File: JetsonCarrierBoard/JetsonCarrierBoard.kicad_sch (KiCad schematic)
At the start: 0 parts

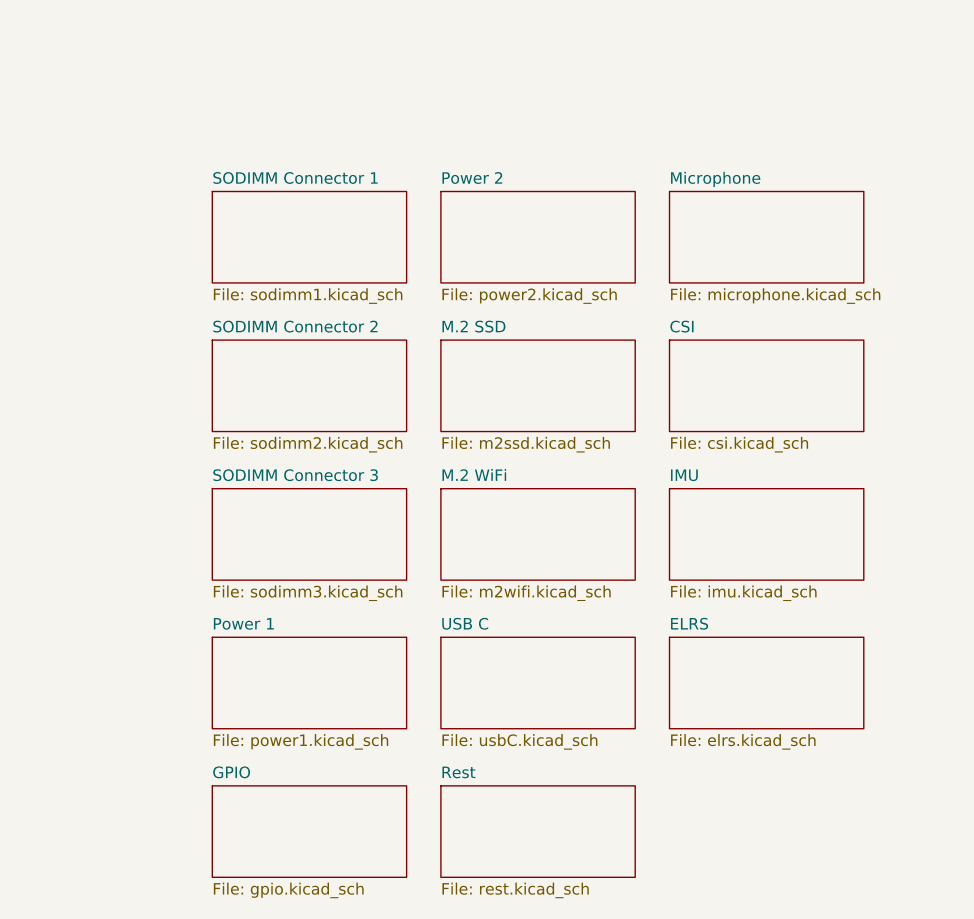
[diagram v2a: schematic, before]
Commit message: Part 2 of USB C wiring, renaming schematics
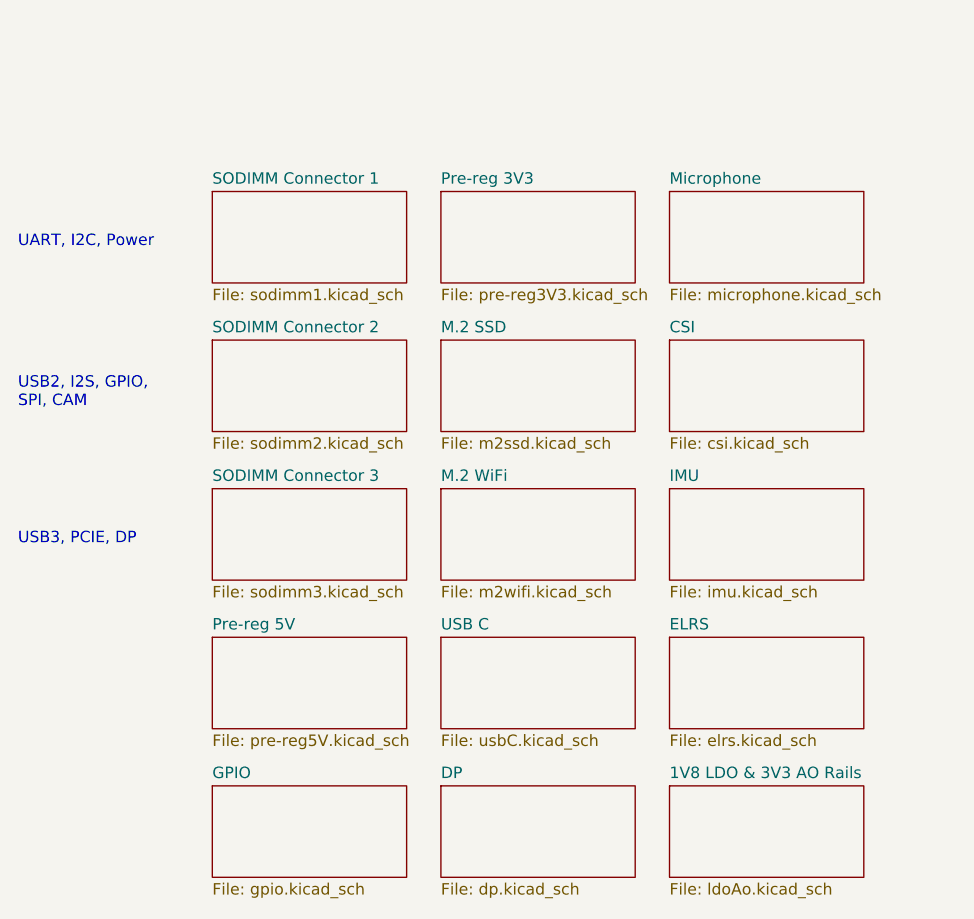
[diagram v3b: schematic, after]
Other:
- sheet Power 1 renamed Pre-reg 5V
- sheet Power 2 renamed Pre-reg 3V3
- sheet Rest renamed DP
- added sheet 1V8 LDO & 3V3 AO Rails (ldoAo.kicad_sch)
- sheet DP: file rest.kicad_sch -> dp.kicad_sch
- sheet Pre-reg 3V3: file power2.kicad_sch -> pre-reg3V3.kicad_sch
- sheet Pre-reg 5V: file power1.kicad_sch -> pre-reg5V.kicad_sch
- note added: "UART, I2C, Power"
- note added: "USB2, I2S, GPIO, SPI, CAM"
- note added: "USB3, PCIE, DP"
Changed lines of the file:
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@@
 (kicad_sch (version 20211123) (generator eeschema)
   (paper "A4")
+  (text "USB2, I2S, GPIO,\nSPI, CAM" (at 95.25 85.09 0)
+    (effects (font (size 1.27 1.27)) (justify left bottom))
+  )
+  (text "USB3, PCIE, DP" (at 95.25 100.33 0)
+    (effects (font (size 1.27 1.27)) (justify left bottom))
+  )
+  (text "UART, I2C, Power" (at 95.25 67.31 0)
+    (effects (font (size 1.27 1.27)) (justify left bottom))
+  )
   (sheet (at 142.24 110.49) (size 21.59 10.16) (fields_autoplaced)
     (stroke (width 0.1524) (type solid) (color 0 0 0 0))
@@
     (stroke (width 0.1524) (type solid) (color 0 0 0 0))
     (fill (color 0 0 0 0.0000))
-    (property "Sheet name" "Rest" (id 0) (at 142.24 126.2884 0)
-      (effects (font (size 1.27 1.27)) (justify left bottom))
-    )
-    (property "Sheet file" "rest.kicad_sch" (id 1) (at 142.24 137.7446 0)
+    (property "Sheet name" "DP" (id 0) (at 142.24 126.2884 0)
+      (effects (font (size 1.27 1.27)) (justify left bottom))
+    )
+    (property "Sheet file" "dp.kicad_sch" (id 1) (at 142.24 137.7446 0)
       (effects (font (size 1.27 1.27)) (justify left top))
     )
@@
     (stroke (width 0.1524) (type solid) (color 0 0 0 0))
     (fill (color 0 0 0 0.0000))
-    (property "Sheet name" "Power 2" (id 0) (at 142.24 60.2484 0)
-      (effects (font (size 1.27 1.27)) (justify left bottom))
-    )
-    (property "Sheet file" "power2.kicad_sch" (id 1) (at 142.24 71.7046 0)
+    (property "Sheet name" "Pre-reg 3V3" (id 0) (at 142.24 60.2484 0)
+      (effects (font (size 1.27 1.27)) (justify left bottom))
+    )
+    (property "Sheet file" "pre-reg3V3.kicad_sch" (id 1) (at 142.24 71.7046 0)
       (effects (font (size 1.27 1.27)) (justify left top))
     )
@@
     (stroke (width 0.1524) (type solid) (color 0 0 0 0))
     (fill (color 0 0 0 0.0000))
-    (property "Sheet name" "Power 1" (id 0) (at 116.84 109.7784 0)
-      (effects (font (size 1.27 1.27)) (justify left bottom))
-    )
-    (property "Sheet file" "power1.kicad_sch" (id 1) (at 116.84 121.2346 0)
+    (property "Sheet name" "Pre-reg 5V" (id 0) (at 116.84 109.7784 0)
+      (effects (font (size 1.27 1.27)) (justify left bottom))
+    )
+    (property "Sheet file" "pre-reg5V.kicad_sch" (id 1) (at 116.84 121.2346 0)
       (effects (font (size 1.27 1.27)) (justify left top))
     )
@@
     )
     (property "Sheet file" "csi.kicad_sch" (id 1) (at 167.64 88.2146 0)
+      (effects (font (size 1.27 1.27)) (justify left top))
+    )
+  )
+  (sheet (at 167.64 127) (size 21.59 10.16) (fields_autoplaced)
+    (stroke (width 0.1524) (type solid) (color 0 0 0 0))
+    (fill (color 0 0 0 0.0000))
+    (property "Sheet name" "1V8 LDO & 3V3 AO Rails" (id 0) (at 167.64 126.2884 0)
+      (effects (font (size 1.27 1.27)) (justify left bottom))
+    )
+    (property "Sheet file" "ldoAo.kicad_sch" (id 1) (at 167.64 137.7446 0)
       (effects (font (size 1.27 1.27)) (justify left top))
     )
@@
     (path "/6dd6e531-721a-4414-9cf5-a3390f309250" (page "14"))
     (path "/35a02f26-4e5e-4a54-87ef-75964a5a411a" (page "15"))
+    (path "/c4aedfda-3c53-45a7-9372-54b9a8f840ba" (page "16"))
   )
   (symbol_instances
-    (path "/7661caa5-a831-4a38-b30b-4546d9bcecdf/0697383b-caf2-42af-bc6d-3eec7a8e6e3d"
-      (reference "#PWR?") (unit 1) (value "+1V8") (footprint "")
-    )
     (path "/c4d380ca-b1d9-4a41-86cf-2b0a86998e0d/09e60d52-849d-4e9f-ae3f-e84e48e8dc21"
       (reference "#PWR?") (unit 1) (value "GND") (footprint "")
@@
     (path "/963f32ba-ec92-4ff1-85dd-63f258059e2d/1386d9a4-71f7-41cd-a560-524abed48850"
       (reference "#PWR?") (unit 1) (value "GND") (footprint "")
+    )
+    (path "/05070324-6f97-4cc0-bdcf-f69bfad6a219/15a6b218-6239-4a6b-9613-e6139914a5c6"
+      (reference "#PWR?") (unit 1) (value "+3.3V") (footprint "")
     )
     (path "/7661caa5-a831-4a38-b30b-4546d9bcecdf/1fae16da-9009-4d63-a296-eaa85652b15b"
@@
       (reference "#PWR?") (unit 1) (value "+3.3V") (footprint "")
     )
-    (path "/7661caa5-a831-4a38-b30b-4546d9bcecdf/5a60a596-f969-4048-b9f0-6c28b54abd9a"
-      (reference "#PWR?") (unit 1) (value "+3.3V") (footprint "")
+    (path "/c4aedfda-3c53-45a7-9372-54b9a8f840ba/5a2d866f-dcb6-43a7-97d0-a02698ce52e6"
+      (reference "#PWR?") (unit 1) (value "+1V8") (footprint "")
+    )
+    (path "/05070324-6f97-4cc0-bdcf-f69bfad6a219/6bda150f-3a32-40ae-a0f8-d9012a1832bc"
+      (reference "#PWR?") (unit 1) (value "GND") (footprint "")
     )
     (path "/7661caa5-a831-4a38-b30b-4546d9bcecdf/75b2df67-f1c8-4922-a8d4-5d0eb1b6eea4"
@@
       (reference "#PWR?") (unit 1) (value "GND") (footprint "")
     )
+    (path "/c4aedfda-3c53-45a7-9372-54b9a8f840ba/bb59e28f-2c75-4121-9867-d2dc70664f7f"
+      (reference "#PWR?") (unit 1) (value "+3.3V") (footprint "")
+    )
+    (path "/c4aedfda-3c53-45a7-9372-54b9a8f840ba/bc7ccac9-6e56-4a2c-bf25-4c95c1121299"
+      (reference "#PWR?") (unit 1) (value "GND") (footprint "")
+    )
     (path "/a2d05d86-0e9b-47b0-b97a-14889aed3931/cf739241-7f9e-4bd9-84c7-298a551b760f"
       (reference "#PWR?") (unit 1) (value "GND") (footprint "")
     )
-    (path "/7661caa5-a831-4a38-b30b-4546d9bcecdf/d0f9fc88-e77e-4f80-bfd3-6861f27fa879"
-      (reference "#PWR?") (unit 1) (value "GND") (footprint "")
-    )
     (path "/fd522664-18f7-41a9-83db-3444870594c0/d424cdad-6034-4fd4-a3b2-c8c7189615cb"
       (reference "#PWR?") (unit 1) (value "GND") (footprint "")
@@
     )
     (path "/05070324-6f97-4cc0-bdcf-f69bfad6a219/e0363390-9312-4b3d-9173-324d0cb811d4"
+      (reference "#PWR?") (unit 1) (value "GND") (footprint "")
+    )
+    (path "/05070324-6f97-4cc0-bdcf-f69bfad6a219/e41ed448-34b7-423b-b572-8fa8b01887a9"
       (reference "#PWR?") (unit 1) (value "GND") (footprint "")
     )
@@
       (reference "C?") (unit 1) (value "0.1u") (footprint "")
     )
+    (path "/05070324-6f97-4cc0-bdcf-f69bfad6a219/4e2886bd-49ab-4698-a872-da0d7e10c965"
+      (reference "C?") (unit 1) (value "C") (footprint "")
+    )
     (path "/c4d380ca-b1d9-4a41-86cf-2b0a86998e0d/616c44f2-bc9f-4390-a1e7-a0df954ba2ec"
       (reference "C?") (unit 1) (value "0.22u") (footprint "")
@@
       (reference "C?") (unit 1) (value "22u") (footprint "")
     )
+    (path "/05070324-6f97-4cc0-bdcf-f69bfad6a219/cae4f632-e432-407a-8bf7-a0a99da561ba"
+      (reference "C?") (unit 1) (value "C") (footprint "")
+    )
     (path "/a2d05d86-0e9b-47b0-b97a-14889aed3931/cca040ec-e059-44dd-956f-79e8ab13c13d"
       (reference "C?") (unit 1) (value "22u") (footprint "")
@@
       (reference "C?") (unit 1) (value "4.7u") (footprint "")
     )
+    (path "/05070324-6f97-4cc0-bdcf-f69bfad6a219/ff8b12bf-4a69-4259-b1f0-038968ec0374"
+      (reference "C?") (unit 1) (value "C") (footprint "")
+    )
+    (path "/05070324-6f97-4cc0-bdcf-f69bfad6a219/ffd2a1ff-3a78-4139-a444-76d5257a8546"
+      (reference "C?") (unit 1) (value "C") (footprint "")
+    )
     (path "/05070324-6f97-4cc0-bdcf-f69bfad6a219/4e802179-b33d-4c16-97cb-ac19e1e95158"
       (reference "J?") (unit 1) (value "USB_C_Receptacle") (footprint "")
@@
       (reference "R?") (unit 1) (value "47k") (footprint "")
     )
+    (path "/05070324-6f97-4cc0-bdcf-f69bfad6a219/6b4bb594-ab55-43e3-9ea5-05bc440f726f"
+      (reference "R?") (unit 1) (value "R") (footprint "")
+    )
     (path "/7661caa5-a831-4a38-b30b-4546d9bcecdf/6f9f91f5-79d1-4717-97da-257cdbe8c0ce"
       (reference "R?") (unit 1) (value "2.2") (footprint "")
@@
       (reference "U?") (unit 1) (value "SIC43x") (footprint "")
     )
-    (path "/7661caa5-a831-4a38-b30b-4546d9bcecdf/16651efc-6dee-47f1-9d26-38d8310f6983"
-      (reference "U?") (unit 1) (value "TLV707") (footprint "")
-    )
     (path "/fd522664-18f7-41a9-83db-3444870594c0/2164f6c1-ad79-41ca-8543-491ce96de329"
       (reference "U?") (unit 1) (value "ICS-43434") (footprint "")
@@
       (reference "U?") (unit 1) (value "ICS-43434") (footprint "")
     )
+    (path "/c4aedfda-3c53-45a7-9372-54b9a8f840ba/a7f2a493-0c9d-4122-99c0-6491746c3f82"
+      (reference "U?") (unit 1) (value "TLV707") (footprint "")
+    )
     (path "/05070324-6f97-4cc0-bdcf-f69bfad6a219/abd012cc-cdc4-41b4-b47e-6430dd835404"

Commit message: Small changes
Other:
- removed sheet ELRS
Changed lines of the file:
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@@
+    )
+  )
+  (sheet (at 116.84 127) (size 21.59 10.16) (fields_autoplaced)
+    (stroke (width 0.1524) (type solid) (color 0 0 0 0))
+    (fill (color 0 0 0 0.0000))
+    (property "Sheet name" "GPIO" (id 0) (at 116.84 126.2884 0)
+      (effects (font (size 1.27 1.27)) (justify left bottom))
+    )
+    (property "Sheet file" "gpio.kicad_sch" (id 1) (at 116.84 137.7446 0)
+      (effects (font (size 1.27 1.27)) (justify left top))
+    )
+  )
+  (sheet (at 116.84 77.47) (size 21.59 10.16) (fields_autoplaced)
+    (stroke (width 0.1524) (type solid) (color 0 0 0 0))
+    (fill (color 0 0 0 0.0000))
+    (property "Sheet name" "SODIMM Connector 2" (id 0) (at 116.84 76.7584 0)
+      (effects (font (size 1.27 1.27)) (justify left bottom))
+    )
+    (property "Sheet file" "sodimm2.kicad_sch" (id 1) (at 116.84 88.2146 0)
+      (effects (font (size 1.27 1.27)) (justify left top))
+    )
+  )
+  (sheet (at 142.24 60.96) (size 21.59 10.16) (fields_autoplaced)
+    (stroke (width 0.1524) (type solid) (color 0 0 0 0))
+    (fill (color 0 0 0 0.0000))
+    (property "Sheet name" "Pre-reg 3V3" (id 0) (at 142.24 60.2484 0)
+      (effects (font (size 1.27 1.27)) (justify left bottom))
+    )
+    (property "Sheet file" "pre-reg3V3.kicad_sch" (id 1) (at 142.24 71.7046 0)
+      (effects (font (size 1.27 1.27)) (justify left top))
+    )
+  )
+  (sheet (at 142.24 93.98) (size 21.59 10.16) (fields_autoplaced)
+    (stroke (width 0.1524) (type solid) (color 0 0 0 0))
+    (fill (color 0 0 0 0.0000))
+    (property "Sheet name" "M.2 WiFi" (id 0) (at 142.24 93.2684 0)
+      (effects (font (size 1.27 1.27)) (justify left bottom))
+    )
+    (property "Sheet file" "m2wifi.kicad_sch" (id 1) (at 142.24 104.7246 0)
+      (effects (font (size 1.27 1.27)) (justify left top))
+    )
+  )
+  (sheet (at 116.84 60.96) (size 21.59 10.16) (fields_autoplaced)
+    (stroke (width 0.1524) (type solid) (color 0 0 0 0))
+    (fill (color 0 0 0 0.0000))
+    (property "Sheet name" "SODIMM Connector 1" (id 0) (at 116.84 60.2484 0)
+      (effects (font (size 1.27 1.27)) (justify left bottom))
+    )
+    (property "Sheet file" "sodimm1.kicad_sch" (id 1) (at 116.84 71.7046 0)
+      (effects (font (size 1.27 1.27)) (justify left top))
+    )
+  )
+  (sheet (at 116.84 110.49) (size 21.59 10.16) (fields_autoplaced)
+    (stroke (width 0.1524) (type solid) (color 0 0 0 0))
+    (fill (color 0 0 0 0.0000))
+    (property "Sheet name" "Pre-reg 5V" (id 0) (at 116.84 109.7784 0)
+      (effects (font (size 1.27 1.27)) (justify left bottom))
+    )
+    (property "Sheet file" "pre-reg5V.kicad_sch" (id 1) (at 116.84 121.2346 0)
+      (effects (font (size 1.27 1.27)) (justify left top))
+    )
+  )
+  (sheet (at 167.64 77.47) (size 21.59 10.16) (fields_autoplaced)
+    (stroke (width 0.1524) (type solid) (color 0 0 0 0))
+    (fill (color 0 0 0 0.0000))
+    (property "Sheet name" "CSI" (id 0) (at 167.64 76.7584 0)
+      (effects (font (size 1.27 1.27)) (justify left bottom))
+    )
+    (property "Sheet file" "csi.kicad_sch" (id 1) (at 167.64 88.2146 0)
+      (effects (font (size 1.27 1.27)) (justify left top))
     )
   )
@@
     (stroke (width 0.1524) (type solid) (color 0 0 0 0))
     (fill (color 0 0 0 0.0000))
-    (property "Sheet name" "ELRS" (id 0) (at 167.64 109.7784 0)
-      (effects (font (size 1.27 1.27)) (justify left bottom))
-    )
-    (property "Sheet file" "elrs.kicad_sch" (id 1) (at 167.64 121.2346 0)
-      (effects (font (size 1.27 1.27)) (justify left top))
-    )
-  )
-  (sheet (at 116.84 127) (size 21.59 10.16) (fields_autoplaced)
-    (stroke (width 0.1524) (type solid) (color 0 0 0 0))
-    (fill (color 0 0 0 0.0000))
-    (property "Sheet name" "GPIO" (id 0) (at 116.84 126.2884 0)
-      (effects (font (size 1.27 1.27)) (justify left bottom))
-    )
-    (property "Sheet file" "gpio.kicad_sch" (id 1) (at 116.84 137.7446 0)
-      (effects (font (size 1.27 1.27)) (justify left top))
-    )
-  )
-  (sheet (at 116.84 77.47) (size 21.59 10.16) (fields_autoplaced)
-    (stroke (width 0.1524) (type solid) (color 0 0 0 0))
-    (fill (color 0 0 0 0.0000))
-    (property "Sheet name" "SODIMM Connector 2" (id 0) (at 116.84 76.7584 0)
-      (effects (font (size 1.27 1.27)) (justify left bottom))
-    )
-    (property "Sheet file" "sodimm2.kicad_sch" (id 1) (at 116.84 88.2146 0)
-      (effects (font (size 1.27 1.27)) (justify left top))
-    )
-  )
-  (sheet (at 142.24 60.96) (size 21.59 10.16) (fields_autoplaced)
-    (stroke (width 0.1524) (type solid) (color 0 0 0 0))
-    (fill (color 0 0 0 0.0000))
-    (property "Sheet name" "Pre-reg 3V3" (id 0) (at 142.24 60.2484 0)
-      (effects (font (size 1.27 1.27)) (justify left bottom))
-    )
-    (property "Sheet file" "pre-reg3V3.kicad_sch" (id 1) (at 142.24 71.7046 0)
-      (effects (font (size 1.27 1.27)) (justify left top))
-    )
-  )
-  (sheet (at 142.24 93.98) (size 21.59 10.16) (fields_autoplaced)
-    (stroke (width 0.1524) (type solid) (color 0 0 0 0))
-    (fill (color 0 0 0 0.0000))
-    (property "Sheet name" "M.2 WiFi" (id 0) (at 142.24 93.2684 0)
-      (effects (font (size 1.27 1.27)) (justify left bottom))
-    )
-    (property "Sheet file" "m2wifi.kicad_sch" (id 1) (at 142.24 104.7246 0)
-      (effects (font (size 1.27 1.27)) (justify left top))
-    )
-  )
-  (sheet (at 116.84 60.96) (size 21.59 10.16) (fields_autoplaced)
-    (stroke (width 0.1524) (type solid) (color 0 0 0 0))
-    (fill (color 0 0 0 0.0000))
-    (property "Sheet name" "SODIMM Connector 1" (id 0) (at 116.84 60.2484 0)
-      (effects (font (size 1.27 1.27)) (justify left bottom))
-    )
-    (property "Sheet file" "sodimm1.kicad_sch" (id 1) (at 116.84 71.7046 0)
-      (effects (font (size 1.27 1.27)) (justify left top))
-    )
-  )
-  (sheet (at 116.84 110.49) (size 21.59 10.16) (fields_autoplaced)
-    (stroke (width 0.1524) (type solid) (color 0 0 0 0))
-    (fill (color 0 0 0 0.0000))
-    (property "Sheet name" "Pre-reg 5V" (id 0) (at 116.84 109.7784 0)
-      (effects (font (size 1.27 1.27)) (justify left bottom))
-    )
-    (property "Sheet file" "pre-reg5V.kicad_sch" (id 1) (at 116.84 121.2346 0)
-      (effects (font (size 1.27 1.27)) (justify left top))
-    )
-  )
-  (sheet (at 167.64 77.47) (size 21.59 10.16) (fields_autoplaced)
-    (stroke (width 0.1524) (type solid) (color 0 0 0 0))
-    (fill (color 0 0 0 0.0000))
-    (property "Sheet name" "CSI" (id 0) (at 167.64 76.7584 0)
-      (effects (font (size 1.27 1.27)) (justify left bottom))
-    )
-    (property "Sheet file" "csi.kicad_sch" (id 1) (at 167.64 88.2146 0)
-      (effects (font (size 1.27 1.27)) (justify left top))
-    )
-  )
-  (sheet (at 167.64 127) (size 21.59 10.16) (fields_autoplaced)
-    (stroke (width 0.1524) (type solid) (color 0 0 0 0))
-    (fill (color 0 0 0 0.0000))
-    (property "Sheet name" "1V8 LDO & 3V3 AO Rails" (id 0) (at 167.64 126.2884 0)
-      (effects (font (size 1.27 1.27)) (justify left bottom))
-    )
-    (property "Sheet file" "ldoAo.kicad_sch" (id 1) (at 167.64 137.7446 0)
+    (property "Sheet name" "1V8 LDO & 3V3 AO Rails" (id 0) (at 167.64 109.7784 0)
+      (effects (font (size 1.27 1.27)) (justify left bottom))
+    )
+    (property "Sheet file" "ldoAo.kicad_sch" (id 1) (at 167.64 121.2346 0)
       (effects (font (size 1.27 1.27)) (justify left top))
     )
@@
     (path "/ae8a82e1-f689-44ad-b6b6-7c67f5a13316" (page "11"))
     (path "/fc058771-52c4-4460-9e1f-f56f767b80ad" (page "12"))
-    (path "/487825d1-d70a-4c12-8e68-8c79fa635e76" (page "13"))
     (path "/6dd6e531-721a-4414-9cf5-a3390f309250" (page "14"))
     (path "/35a02f26-4e5e-4a54-87ef-75964a5a411a" (page "15"))
@@
       (reference "#PWR?") (unit 1) (value "GND") (footprint "")
     )
+    (path "/963f32ba-ec92-4ff1-85dd-63f258059e2d/614ea1df-89f1-41a8-b073-c383ea7276a7"
+      (reference "#PWR?") (unit 1) (value "GND") (footprint "")
+    )
     (path "/05070324-6f97-4cc0-bdcf-f69bfad6a219/6d9b7148-bc8d-45e2-b1ab-759efc40aa7b"
       (reference "#PWR?") (unit 1) (value "+5V") (footprint "")
@@
       (reference "C?") (unit 1) (value "10u") (footprint "")
     )
+    (path "/963f32ba-ec92-4ff1-85dd-63f258059e2d/76fa9c11-f466-4a8b-b52d-e35c124b0743"
+      (reference "C?") (unit 1) (value "560u") (footprint "")
+    )
     (path "/a2d05d86-0e9b-47b0-b97a-14889aed3931/77134455-401a-4cc3-bf4a-59ed8186ceda"
       (reference "C?") (unit 1) (value "0.1u") (footprint "")
+    )
+    (path "/963f32ba-ec92-4ff1-85dd-63f258059e2d/77eefc19-4a42-43bb-85bf-9b4a9557485d"
+      (reference "C?") (unit 1) (value "100u") (footprint "")
     )
     (path "/a2d05d86-0e9b-47b0-b97a-14889aed3931/800a232e-3f7c-4a16-bf9c-290c495bb410"
@@
       (reference "C?") (unit 1) (value "10n") (footprint "")
     )
+    (path "/963f32ba-ec92-4ff1-85dd-63f258059e2d/ae20ef7e-56bb-47fe-8e7b-d2953aab6853"
+      (reference "C?") (unit 1) (value "100u") (footprint "")
+    )
     (path "/77e90ef4-3018-4848-8164-832394b45da9/b1812e93-6d07-48bc-8440-4307c7b13cf3"

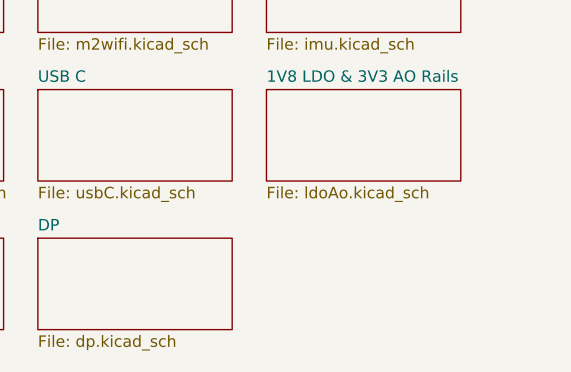
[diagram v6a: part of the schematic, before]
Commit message: Power Sequencing Wiring Part 1
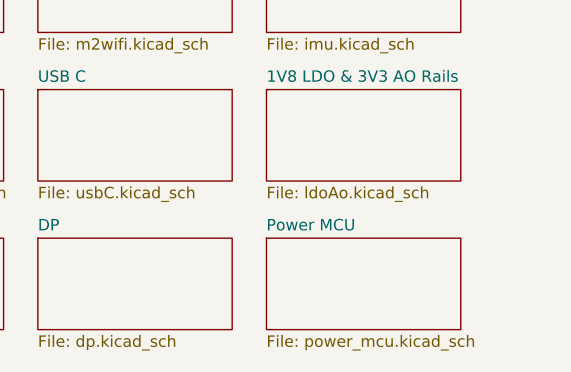
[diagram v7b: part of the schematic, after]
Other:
- added sheet Power MCU (power_mcu.kicad_sch)
